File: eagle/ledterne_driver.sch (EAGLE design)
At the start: 10 parts, among them IC1 MEGA8-AI

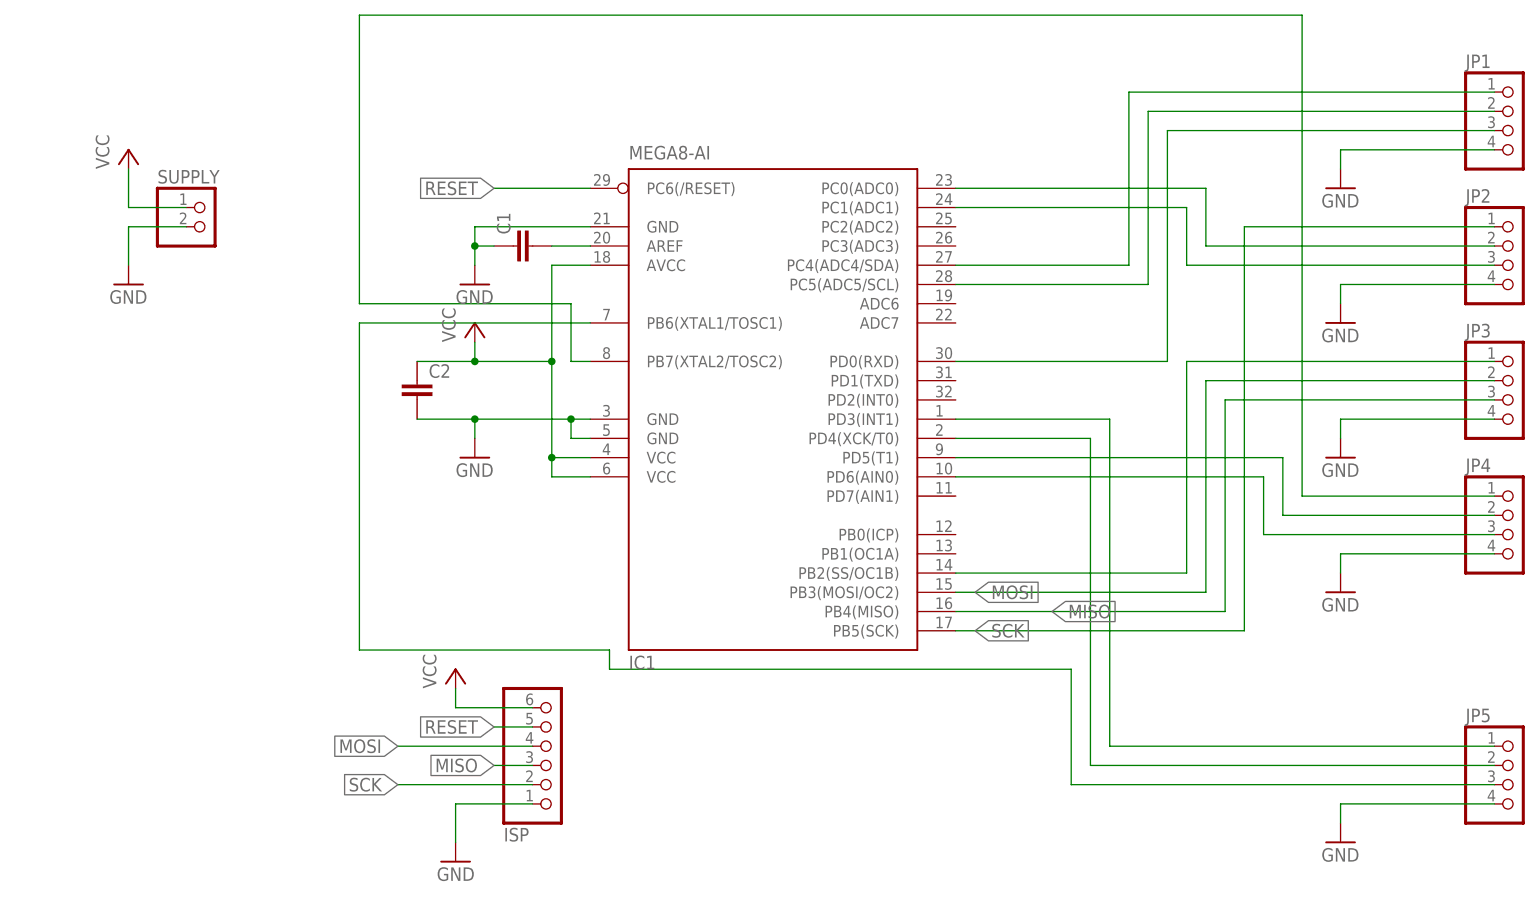
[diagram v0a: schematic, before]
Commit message: Alternative routing for driver board
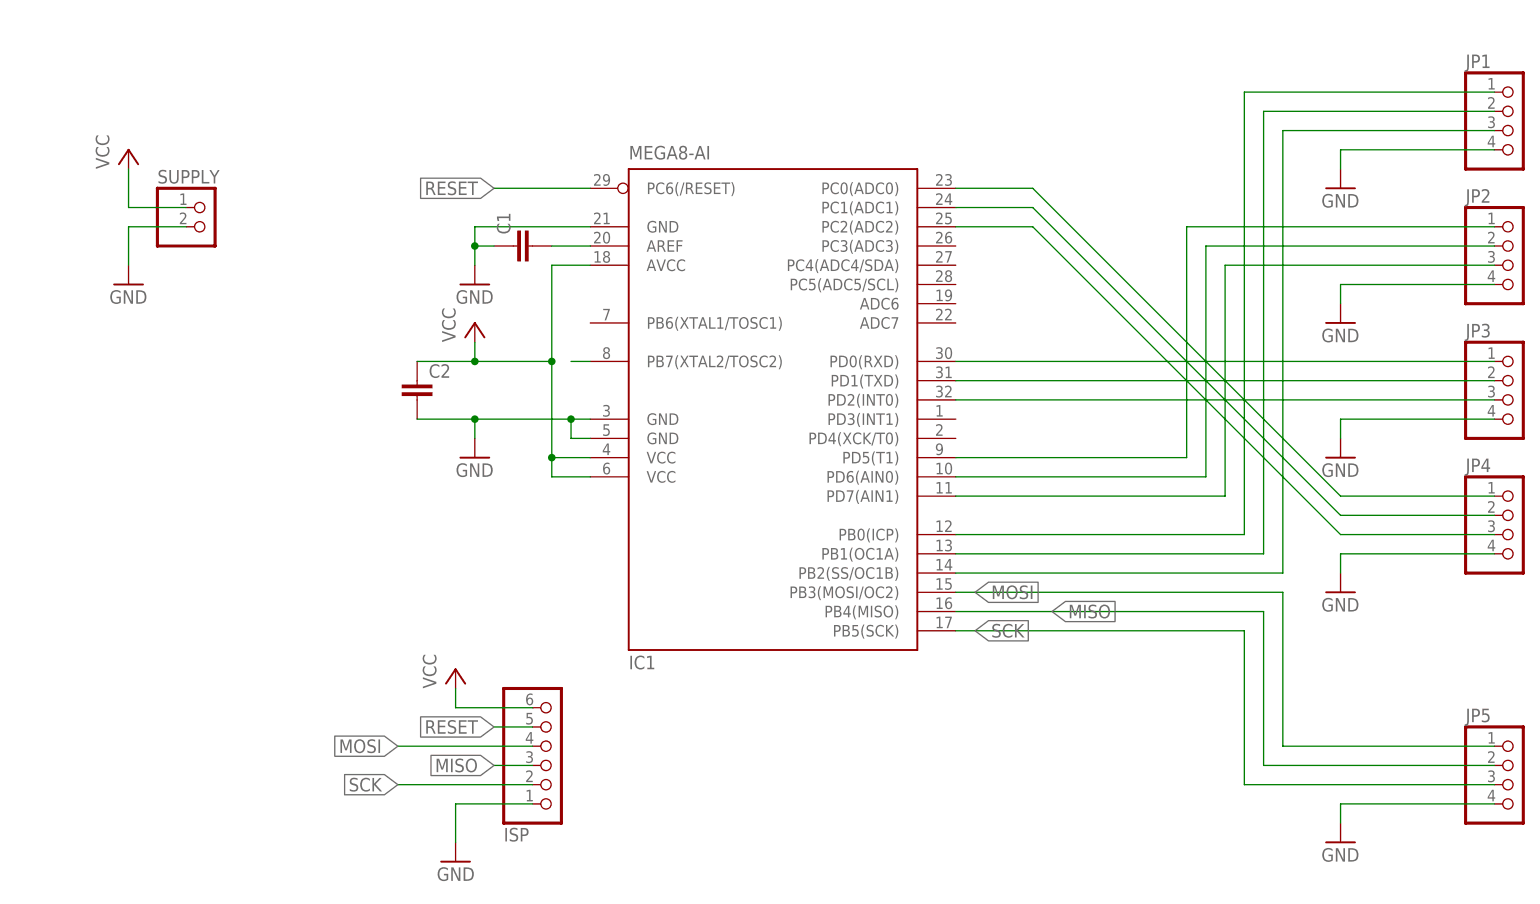
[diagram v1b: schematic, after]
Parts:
- C1, C2: device rcl:C-EUC0603 -> rcl:C-EUC0603K
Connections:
- removed net N$2: IC1.PD0(RXD), JP1.3
- new net N$14: IC1.PB7(XTAL2/TOSC2)
- new net N$15: IC1.PC2(ADC2), JP4.3
- net MISO: now also JP5.2; no longer JP3.3
- net MOSI: now also JP5.1; no longer JP3.2
- net N$10: now also IC1.PD1(TXD), JP3.2; no longer IC1.PD6(AIN0), JP4.3
- net N$11: now also IC1.PD2(INT0), JP3.3; no longer IC1.PB6(XTAL1/TOSC1), JP5.3
- net N$12: now also IC1.PC0(ADC0); no longer IC1.PB7(XTAL2/TOSC2)
- net N$13: now also IC1.PC1(ADC1), JP4.2; no longer IC1.PD3(INT1), JP5.1
- net N$3: now also IC1.PB2(SS/OC1B), JP1.3; no longer IC1.PC5(ADC5/SCL), JP1.2
- net N$4: now also IC1.PB1(OC1A), JP1.2; no longer IC1.PC4(ADC4/SDA), JP1.1
- net N$5: now also IC1.PB0(ICP), JP1.1; no longer IC1.PC0(ADC0), JP2.2
- net N$6: now also IC1.PD7(AIN1), JP2.3; no longer IC1.PD4(XCK/T0), JP5.2
- net N$7: now also IC1.PD6(AIN0), JP2.2; no longer IC1.PC1(ADC1), JP2.3
- net N$8: now also IC1.PD5(T1), JP2.1; no longer IC1.PB2(SS/OC1B), JP3.1
- net N$9: now also IC1.PD0(RXD), JP3.1; no longer IC1.PD5(T1), JP4.2
- net SCK: now also JP5.3; no longer JP2.1

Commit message: Replace ISP connector with solder pads
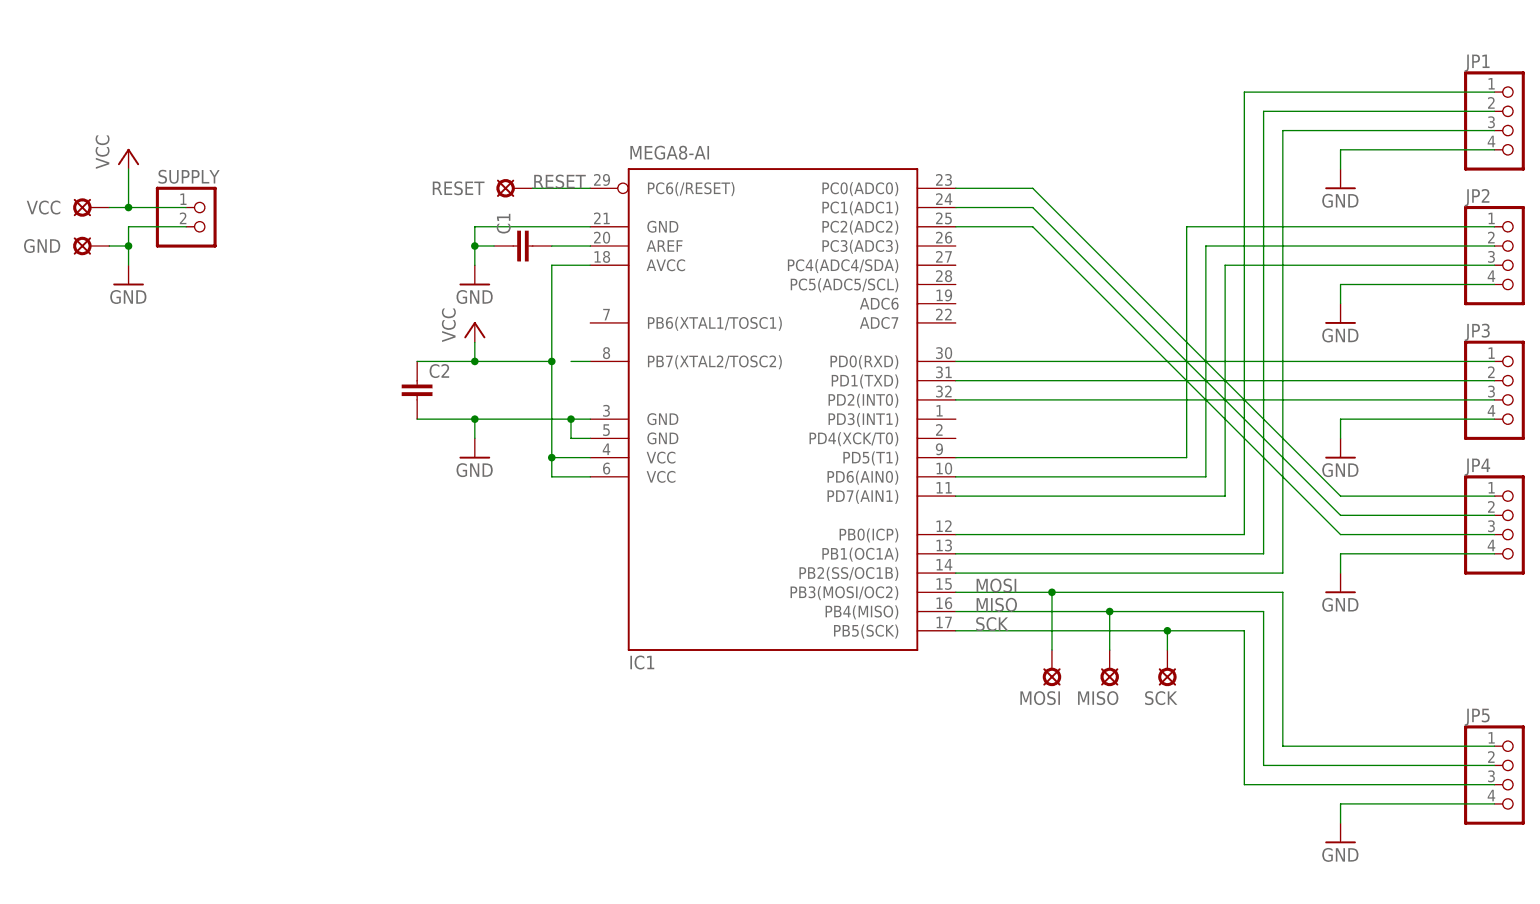
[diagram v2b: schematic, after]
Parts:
- removed ISP: (no value), pinhead:PINHD-1X6
- added GND, MISO, MOSI, RESET, SCK, VCC: SOLPAD-SMD-NORMAL, solpad-smd:SOLPAD-SMD-NORMAL
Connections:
- net GND: now also GND.MP; no longer ISP.1
- net MISO: now also MISO.MP; no longer ISP.3
- net MOSI: now also MOSI.MP; no longer ISP.4
- net RESET: now also RESET.MP; no longer ISP.5
- net SCK: now also SCK.MP; no longer ISP.2
- net VCC: now also VCC.MP; no longer ISP.6
